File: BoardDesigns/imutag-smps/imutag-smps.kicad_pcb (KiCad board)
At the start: 4 copper layers, 21.5 x 11.5 mm, 36 parts, among them J201 CONN_02X04, J301 Conn_01x01, J302 Conn_01x01, J303 Conn_01x01, J304 Conn_01x01, J401 CONN_01X02, Q501 PMBT2222AMBYL, U1 TPS22916BYFPR, U2 BMM350, U3 BMP581, U302 stm32U375, U4 TPS62840YBGR, U5 LSM6DSV, U501 RV-3028-C8, U6 GD5F2GM7REYIGR

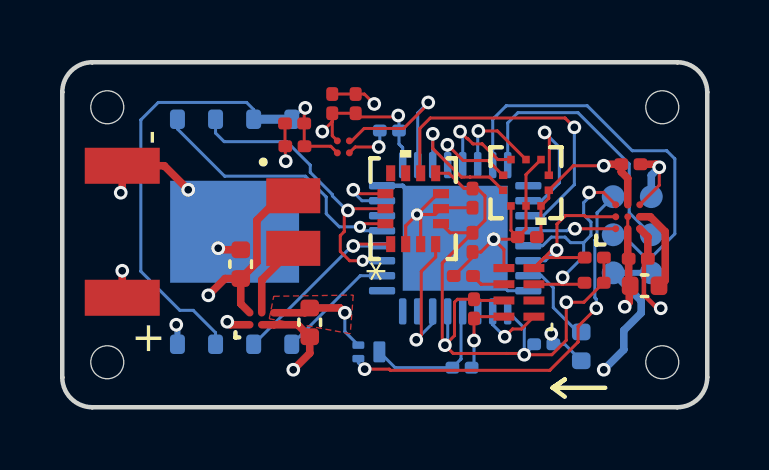
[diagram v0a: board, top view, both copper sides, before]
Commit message: imutag-smps: design review 2 — switching converter, magnetics, pin map
Review of the SMPS power stage and the current board state, following 2026-08-26.
NOT ordered: one architectural question is still open.

Board changes
- L1 reroute: /AT25_MOSI on B.Cu moved 1.13 -> 1.38 mm from the inductor centre,
  now clear of the 1.6 x 2.0 mm body outline; /AT25_SCK 1.57 -> 1.69 mm.
- BMP581 symbol updated from the library: VSS pins 3/8/9 were typed power_out where
  libraries:BMP581 has power_in. That silently drove the GND net; correcting it
  exposed power_pin_not_driven on U1 pin B1 - the same latent bug as
  RV-3028-C7-AccelTag on imutag-nand-bmp581. Fixed with a PWR_FLAG (#FLG02) on GND.
- #FLG01 moved from /Flash 1V8, which U1's VOUT already drives, to +1V8, which the
  TPS62840 symbol leaves undriven because VOS is correctly typed as a sense input.
  That cleared both remaining ERC errors.
- Edge clearance and annular ring brought in line with the sibling: inner copper
  0.3005 mm from the profile, all 47 vias at 0.1524 mm (6.00 mil), single drill.

Verified: DRC 0 violations / 0 unconnected / 0 parity. ERC 0 violations, and 0
errors with all 24 exclusions cleared. Export 2026-09-02-08-29-52 matches the board
- 300/300 fill vertices on both inner planes, 412/412 track starts, PTH 47 = 47
vias, NPTH 4. Superseded exports pruned; the gerber archive is force-added past the
repo-wide *.zip rule so the package is recoverable from the commit.

Findings
1. The TPS62840YBG has NO MODE pin - datasheet 8.3.3, "not available in the YBG
   package". Forced PWM is unavailable, so at 1-2.2 mA the converter sits in PFM
   and switching noise is bursty, load-dependent and not selectable. This removes
   the option the family-level SMPS-vs-LDO decision rested on: the buck keeps its
   full ~1.85x battery-life advantage precisely because the mode that would have
   erased it cannot be chosen. Not a defect - a decision to make deliberately.
2. Switching-loop layout reviewed, the item R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
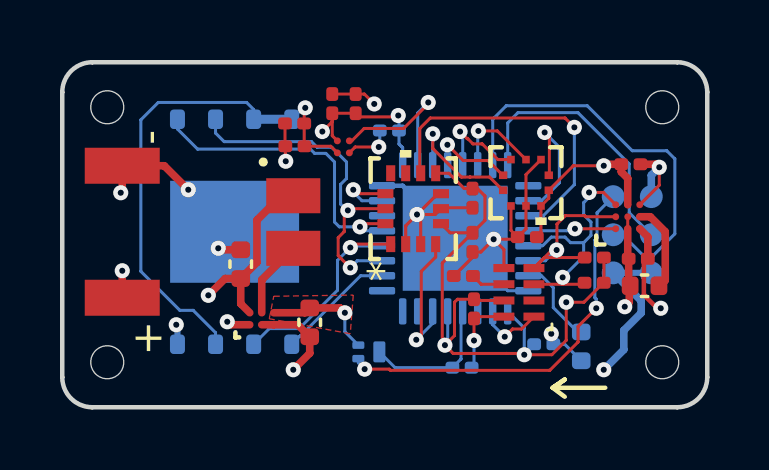
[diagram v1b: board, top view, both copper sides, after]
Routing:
- net /AT25_SCK: track 10.7 -> 11.9 mm
- net /AT25_MOSI: track 9.93 -> 10.8 mm
- net /AT25_MISO: track 7.01 -> 7.61 mm

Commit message: imutag-smps: pin alternates, tighter DRC, symbol hygiene; prune to current outputs
Continues the 2026-09-02 review. Still NOT ordered - finding 1 (the TPS62840YBG has
no MODE pin, so the converter is PFM-only) remains the open architectural question.

Design
- All 12 U302 pin alternates declared on the schematic, so pin intent is stated by
  the design rather than inferred by the reviewer. PB4 is LPTIM1_CH2, not a GPIO;
  PC14 is RCC_OSC32_IN, feeding the LSE in bypass mode from the RV-3028's 32.768 kHz
  CLKOUT. LPTIM1 divides that onto PB4 to trigger the IMU in hardware while the CPU
  is stopped, at 1 PPM rather than internal-RC accuracy.
- RV-3028 CLKOUT retyped input -> output, in the library and the schematic cache.
  Correct direction and required for coherence with PC14 declaring RCC_OSC32_IN.
- BMP581 symbol updated from library; pin maps now identical, VSS pins power_in.
- U501 repointed tag_library:RV-3028-C7 -> libraries:RV-3028-C7. 'tag_library' is not
  in this project's sym-lib-table and resolved only through the user-level table, so
  the reference was machine-local and would fail on a fresh clone while ERC stayed
  quiet - the cached lib_symbols entry hides it. Connectivity verified unchanged:
  37 nets, 138 pin connections.
- DRC severities tightened: npth_inside_courtyard and pth_inside_courtyard
  ignore -> warning, track_not_centered_on_via ignore -> ERROR. The last matters
  because the board was moved to a 6.00 mil annular ring for margin, which an
  off-centre track endpoint would silently give back.

Verified: DRC 0 violations / 0 unconnected / 0 parity with the tightened rules. ERC
0 violations, and 0 errors with all 17 exclusions cleared. Promoting every remaining
'ignore' yields only 5 missing_courtyard hits, all on mounting holes and battery
lands. Export 2026-09-03-07-51-02 matches the board: 300/300 fill vertices on both
inner planes, 392/392 track starts, edge 0.3005 mm, PTH 44 = 44 vias, BOM 16 lines /
27 placements matching the CPL.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
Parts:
- removed C10: 1uf, Capacitor_SMD:C_0201_0603Metric
- removed C507: 0.1uf, Capacitor_SMD:C_0201_0603Metric
- removed U1: TPS22916BYFPR, libraries:IC_TPS22916BYFPR
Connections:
- C11 pad 1: /Flash 1V8 -> +1V8
- C504 pad 1: /Flash 1V8 -> +1V8
- U302 pad 18: /FLASH_PWR -> unconnected-(U302-PA8-Pad18)
- U6 pad 3: /Flash 1V8 -> +1V8
- U6 pad 7: /Flash 1V8 -> +1V8
- U6 pad 8: /Flash 1V8 -> +1V8
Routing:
- net /Flash 1V8: track 17.6 -> 0.00 mm, vias 1 -> 0
- net +1V8: track 44.6 -> 57.1 mm
- net /FLASH_PWR: track 5.42 -> 0.00 mm, vias 1 -> 0
- net GND: track 48.6 -> 46.1 mm, vias 15 -> 14
